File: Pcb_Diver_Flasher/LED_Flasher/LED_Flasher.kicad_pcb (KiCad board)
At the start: 2 copper layers, 105 x 20 mm, 35 parts, among them IC101 PIC16LF15313, J101 SKEDD6, SW101 MK15-C2, T101 BUK7880-55A, T102 BUK7880-55A

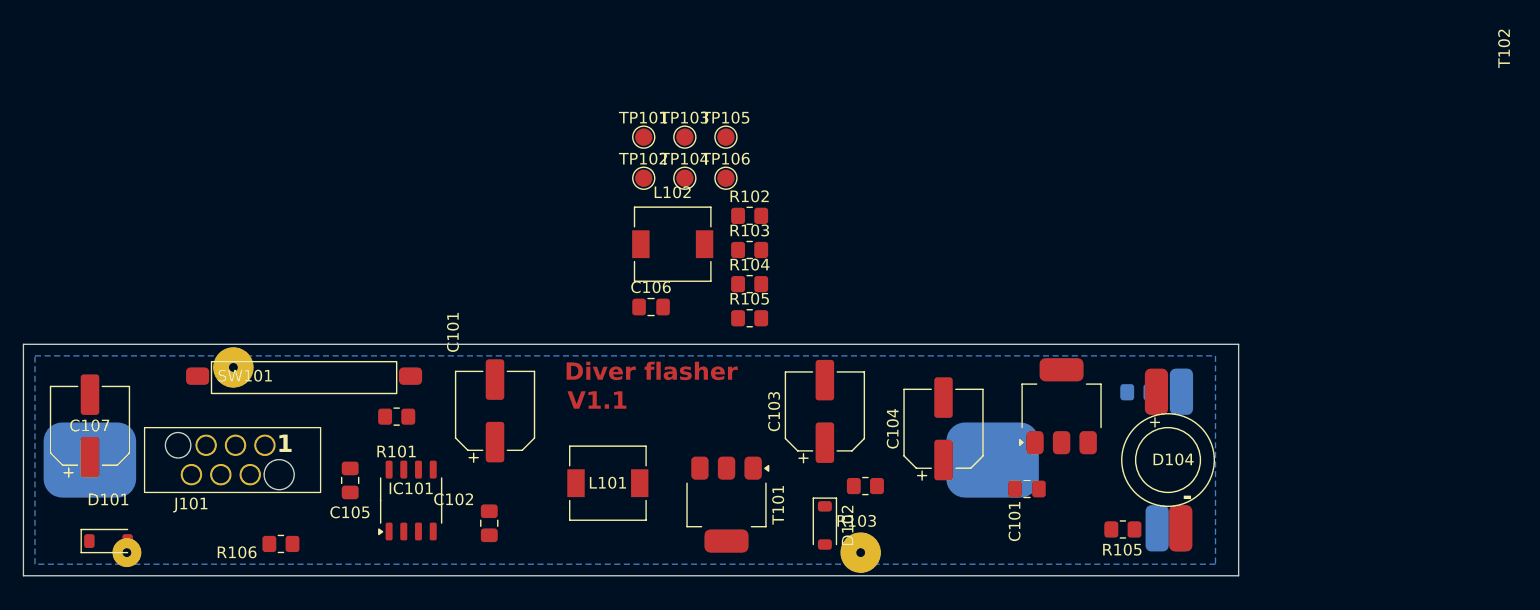
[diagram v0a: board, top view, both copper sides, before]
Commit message: Old PC (v1) removed Latest changes for current schematic routed. Almost ready DRC outstanding.
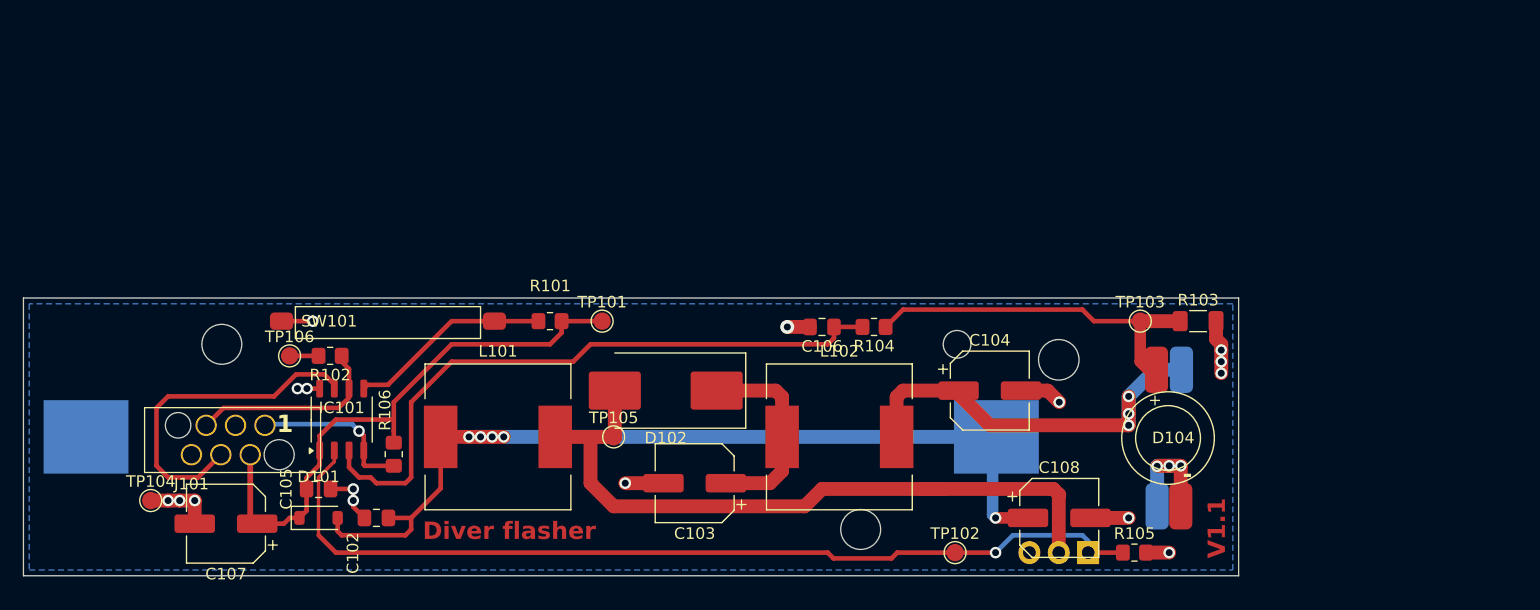
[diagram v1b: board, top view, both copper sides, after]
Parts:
- removed C101: 47µF/10V, Capacitor_SMD:CP_Elec_6.3x7.7
- removed C101: 330nF, Capacitor_SMD:C_0805_2012Metric_Pad1.18x1.45mm_HandSolder
- removed the R103 at (112.8, 91.8)
- removed the R103 at (122.8, 112.2)
- removed the R104 at (112.8, 94.8)
- removed the R104 at (146.4, 104.1)
- removed the R105 at (145.0, 116.0)
- removed the R105 at (112.8, 97.8)
- removed T102: BUK7880-55A, Package_TO_SOT_SMD:SOT-223-3_TabPin2
- added C108: 100µF/16V, Capacitor_SMD:CP_Elec_6.3x5.8, F.Cu at (139.5, 115.0)
- added R103: 1, Resistor_SMD:R_1206_3216Metric_Pad1.30x1.75mm_HandSolder, F.Cu at (151.5, 98.0)
- added R104: 1K, Resistor_SMD:R_0805_2012Metric_Pad1.20x1.40mm_HandSolder, F.Cu at (123.5, 98.5)
- added R105: 100K, Resistor_SMD:R_0805_2012Metric_Pad1.20x1.40mm_HandSolder, F.Cu at (146.0, 118.0)
- BAT101: footprint MyPower:KEYSTONE_1042 -> Battery:BatteryHolder_Keystone_1042_1x18650
- C103, C104, C107: value 100µF/10V -> 100µF/16V; footprint Capacitor_SMD:CP_Elec_6.3x7.7 -> Capacitor_SMD:CP_Elec_6.3x5.8
- D102: value BAV16W -> SL42; footprint Diode_SMD:D_SOD-123 -> Diode_SMD:D_SMC_Handsoldering
- L101, L102: footprint Inductor_SMD:L_6.3x6.3_H3 -> Inductor_SMD:L_12x12mm_H8mm
- T101: value BUK7880-55A -> DMT6009LCT; footprint Package_TO_SOT_SMD:SOT-223-3_TabPin2 -> Package_TO_SOT_THT:TO-220-3_Horizontal_TabDown; moved to B.Cu
- moved TP104 53.9 mm to (61.0, 113.5)
- moved TP103 42.4 mm to (146.5, 98.0)
- moved TP102 42.1 mm to (130.5, 118.0)
- moved TP106 40.7 mm to (73.0, 101.0)
- moved R102 38.2 mm to (76.5, 101.0), turned to 180 degrees
- moved T101 31.5 mm to (142.0, 118.0), turned to 180 degrees
- moved TP105 27.7 mm to (101.0, 108.0)
- moved L102 22.0 mm to (120.5, 108.0)
- moved D101 18.3 mm to (75.5, 115.0)
- moved D102 18.0 mm to (105.5, 104.0), turned to 180 degrees
- moved TP101 16.3 mm to (100.0, 98.0)
- moved R101 15.6 mm to (95.5, 98.0), turned to 180 degrees
- moved C106 14.9 mm to (119.0, 98.5), turned to 180 degrees
- moved C107 14.5 mm to (67.5, 115.5), turned to 180 degrees
- moved C103 12.8 mm to (108.0, 112.0), turned to 180 degrees
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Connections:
- net Net-(D102-K) renamed /Boost
- net Net-(D103-K) renamed /LED
- D104 pad 1: Net-(D104-K) -> /Shunt
- TP103 pad 1: /Current -> /Shunt
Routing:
- net /Switch: track 0.00 -> 80.3 mm, vias 0 -> 1
- net +BATT: track 0.00 -> 79.3 mm, vias 0 -> 5
- net /SW_OUT: track 0.00 -> 62.3 mm
- net /Current: track 0.00 -> 56.4 mm
- net /PWR_MCU: track 0.00 -> 49.9 mm
- net /LED_PWR: track 0.00 -> 35.7 mm, vias 0 -> 3
- net GND: track 0.00 -> 34.5 mm, vias 0 -> 16
- net /Shunt: track 0.00 -> 31.7 mm
- net /ICSPDAT: track 0.00 -> 29.7 mm
- net /Boost: track 0.00 -> 17.6 mm
- net /Reed_In: track 0.00 -> 17.5 mm
- net /ICSPCLK: track 0.00 -> 17.2 mm
- net /MCLR!: track 0.00 -> 14.1 mm, vias 0 -> 1
- net /LED: track 0.00 -> 11.0 mm, vias 0 -> 3
- net /DEBUG: track 0.00 -> 2.50 mm
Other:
- board size 105 x 20 mm -> 105 x 24 mm
